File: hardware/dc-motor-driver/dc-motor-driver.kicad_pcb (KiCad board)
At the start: 2 copper layers, 100 x 100 mm, 69 parts, among them J1 DE9, J10 MOT, J12 MOT, J14 MOT, J2 VCC, J4 MOT, J6 MOT, J8 MOT, U1 DRV8874PWPR, U2 DRV8874PWPR, U3 DRV8874PWPR, U4 DRV8874PWPR, U5 DRV8874PWPR, U6 DRV8874PWPR

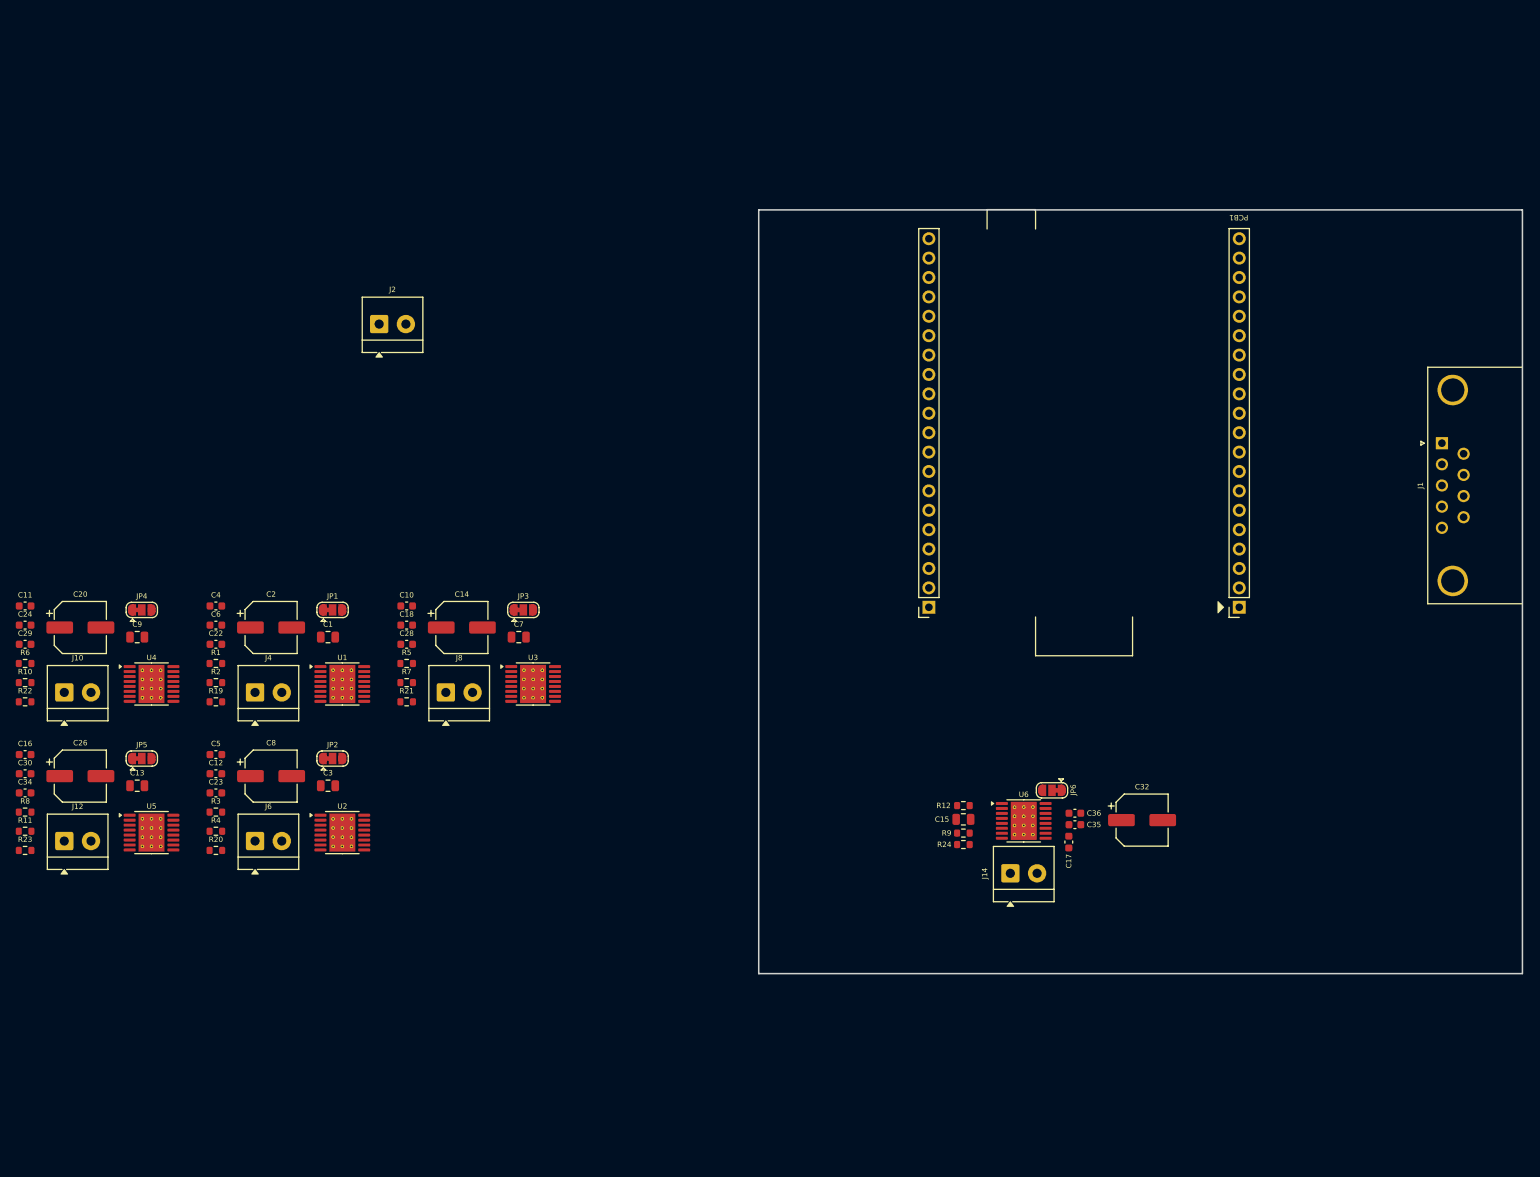
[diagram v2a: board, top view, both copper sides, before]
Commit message: Initial H-Bridge layout with SB footprint added
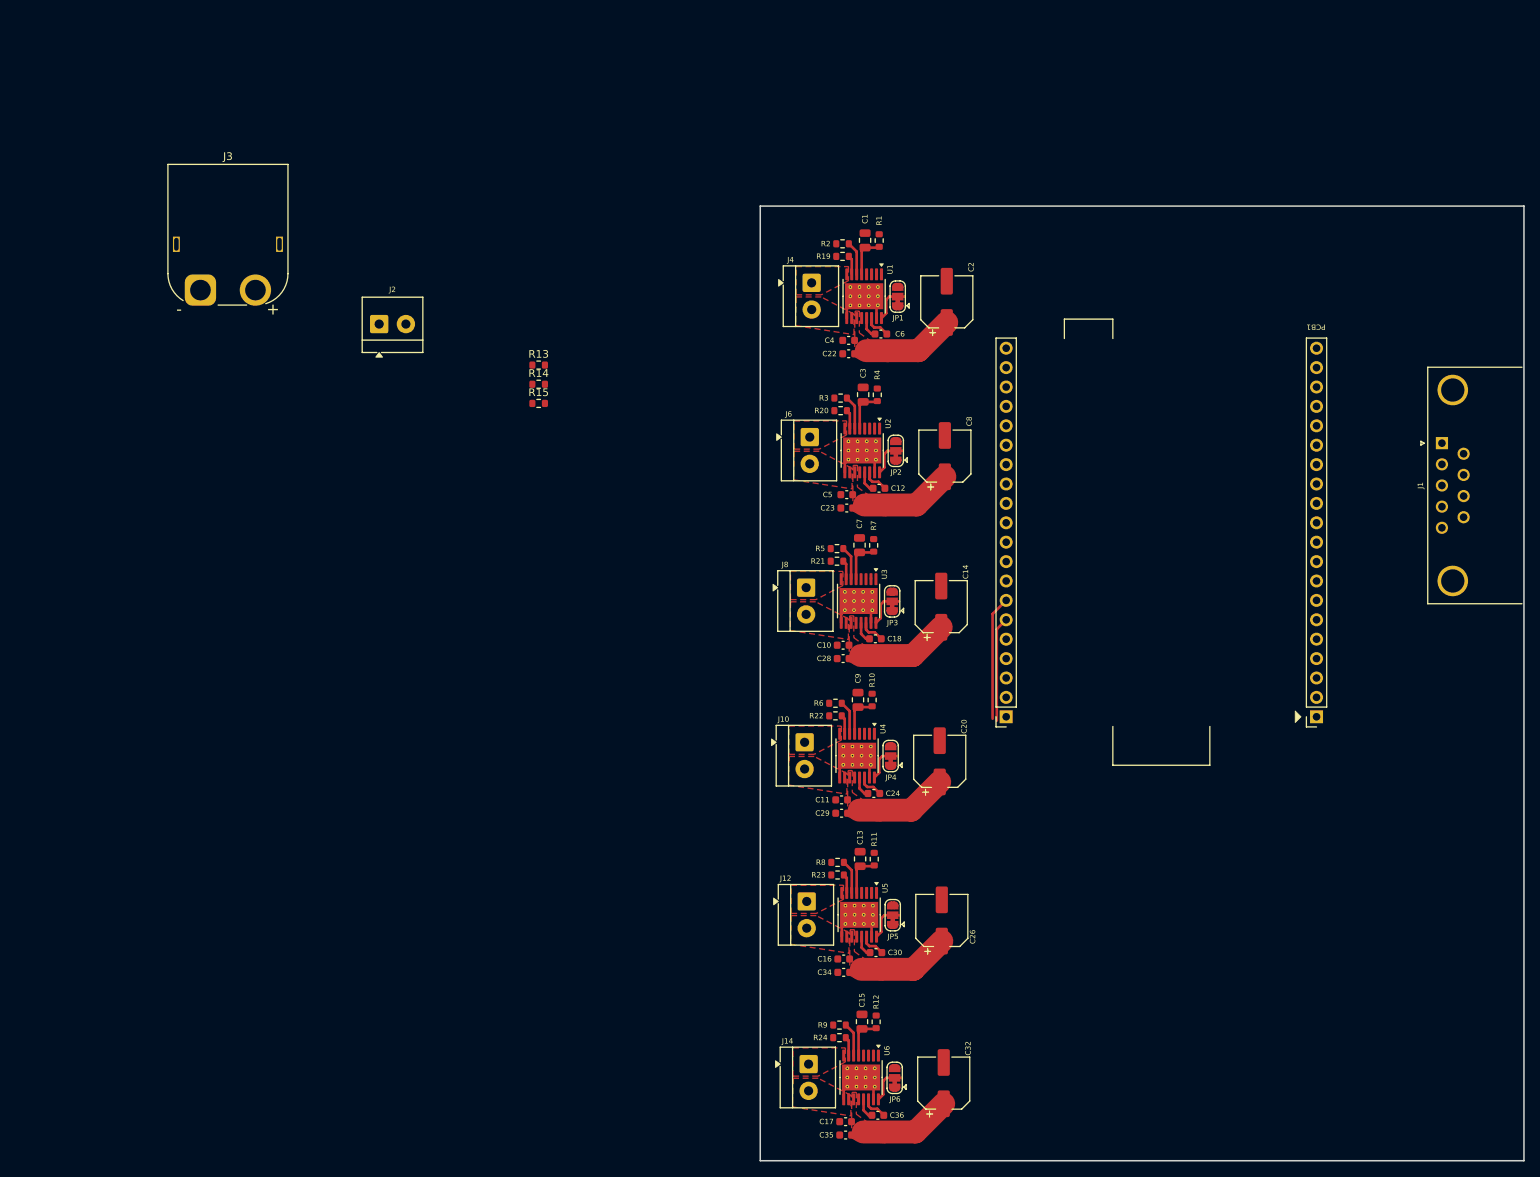
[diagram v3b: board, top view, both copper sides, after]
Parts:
- added J3: Conn_01x02, Connector_AMASS:AMASS_XT60PW-M_1x02_P7.20mm_Horizontal, F.Cu at (42.2, 53.4)
- added R13: 10k, Resistor_SMD:R_0603_1608Metric, F.Cu at (86.5, 63.2)
- added R14: 10k, Resistor_SMD:R_0603_1608Metric, F.Cu at (86.5, 65.7)
- added R15: 10k, Resistor_SMD:R_0603_1608Metric, F.Cu at (86.5, 68.2)
- J2: value VCC -> VIN
- moved C26 114.4 mm to (139.3, 135.9), turned to 90 degrees
- moved C20 113.9 mm to (139.0, 115.1), turned to 90 degrees
- moved C30 113.8 mm to (130.7, 140.2)
- moved C24 113.3 mm to (130.4, 119.3)
- moved R11 111.2 mm to (130.4, 127.9), turned to -90 degrees
- moved R10 110.9 mm to (130.2, 107.1), turned to -90 degrees
- moved C16 110.5 mm to (126.4, 141.0), turned to 180 degrees
- moved C11 109.9 mm to (126.2, 120.2), turned to 180 degrees
- moved C34 109.7 mm to (126.4, 142.7), turned to 180 degrees
- moved C29 109.2 mm to (126.2, 121.9), turned to 180 degrees
- moved R8 106.6 mm to (125.6, 128.3), turned to 180 degrees
- moved R23 106.4 mm to (125.6, 130.0), turned to 180 degrees
- moved R6 106.2 mm to (125.3, 107.5), turned to 180 degrees
- moved R22 106.1 mm to (125.3, 109.2), turned to 180 degrees
- moved R4 103.8 mm to (130.8, 67.1), turned to -90 degrees
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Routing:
- net VCC: track 0.00 -> 72.5 mm
- net GND: track 0.00 -> 21.6 mm
- net /MOT6_IN2: track 0.00 -> 16.4 mm
- net /MOT6_IN1: track 0.00 -> 13.7 mm
- net /BANK1_I_SENSE: track 0.00 -> 8.85 mm
- net /BANK2_I_SENSE: track 0.00 -> 8.85 mm
- net /BANK3_I_SENSE: track 0.00 -> 8.85 mm
- net Net-(U5-VREF): track 0.00 -> 5.58 mm
- net Net-(U4-VREF): track 0.00 -> 5.58 mm
- net Net-(U6-VREF): track 0.00 -> 5.58 mm
- net Net-(U1-VREF): track 0.00 -> 5.58 mm
- net Net-(U3-VREF): track 0.00 -> 5.58 mm
- net Net-(U2-VREF): track 0.00 -> 5.58 mm
- net Net-(JP3-C): track 0.00 -> 5.20 mm
- net Net-(JP6-C): track 0.00 -> 5.20 mm
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- added copper zone on F.Cu, net Net-(J10-Pin_1)
- added copper zone on F.Cu, net Net-(J10-Pin_2)
- added copper zone on F.Cu, net Net-(J12-Pin_1)
- added copper zone on F.Cu, net Net-(J12-Pin_2)
- added copper zone on F.Cu, net Net-(J14-Pin_1)
- added copper zone on F.Cu, net Net-(J14-Pin_2)
- added copper zone on F.Cu, net Net-(J4-Pin_1)
- added copper zone on F.Cu, net Net-(J4-Pin_2)
- added copper zone on F.Cu, net Net-(J6-Pin_1)
- added copper zone on F.Cu, net Net-(J6-Pin_2)
- added copper zone on F.Cu, net Net-(J8-Pin_1)
- added copper zone on F.Cu, net Net-(J8-Pin_2)
- added copper zone on F.Cu, net VCC
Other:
- board size 100 x 100 mm -> 100 x 125 mm

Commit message: feat: DRC rules, more layout done
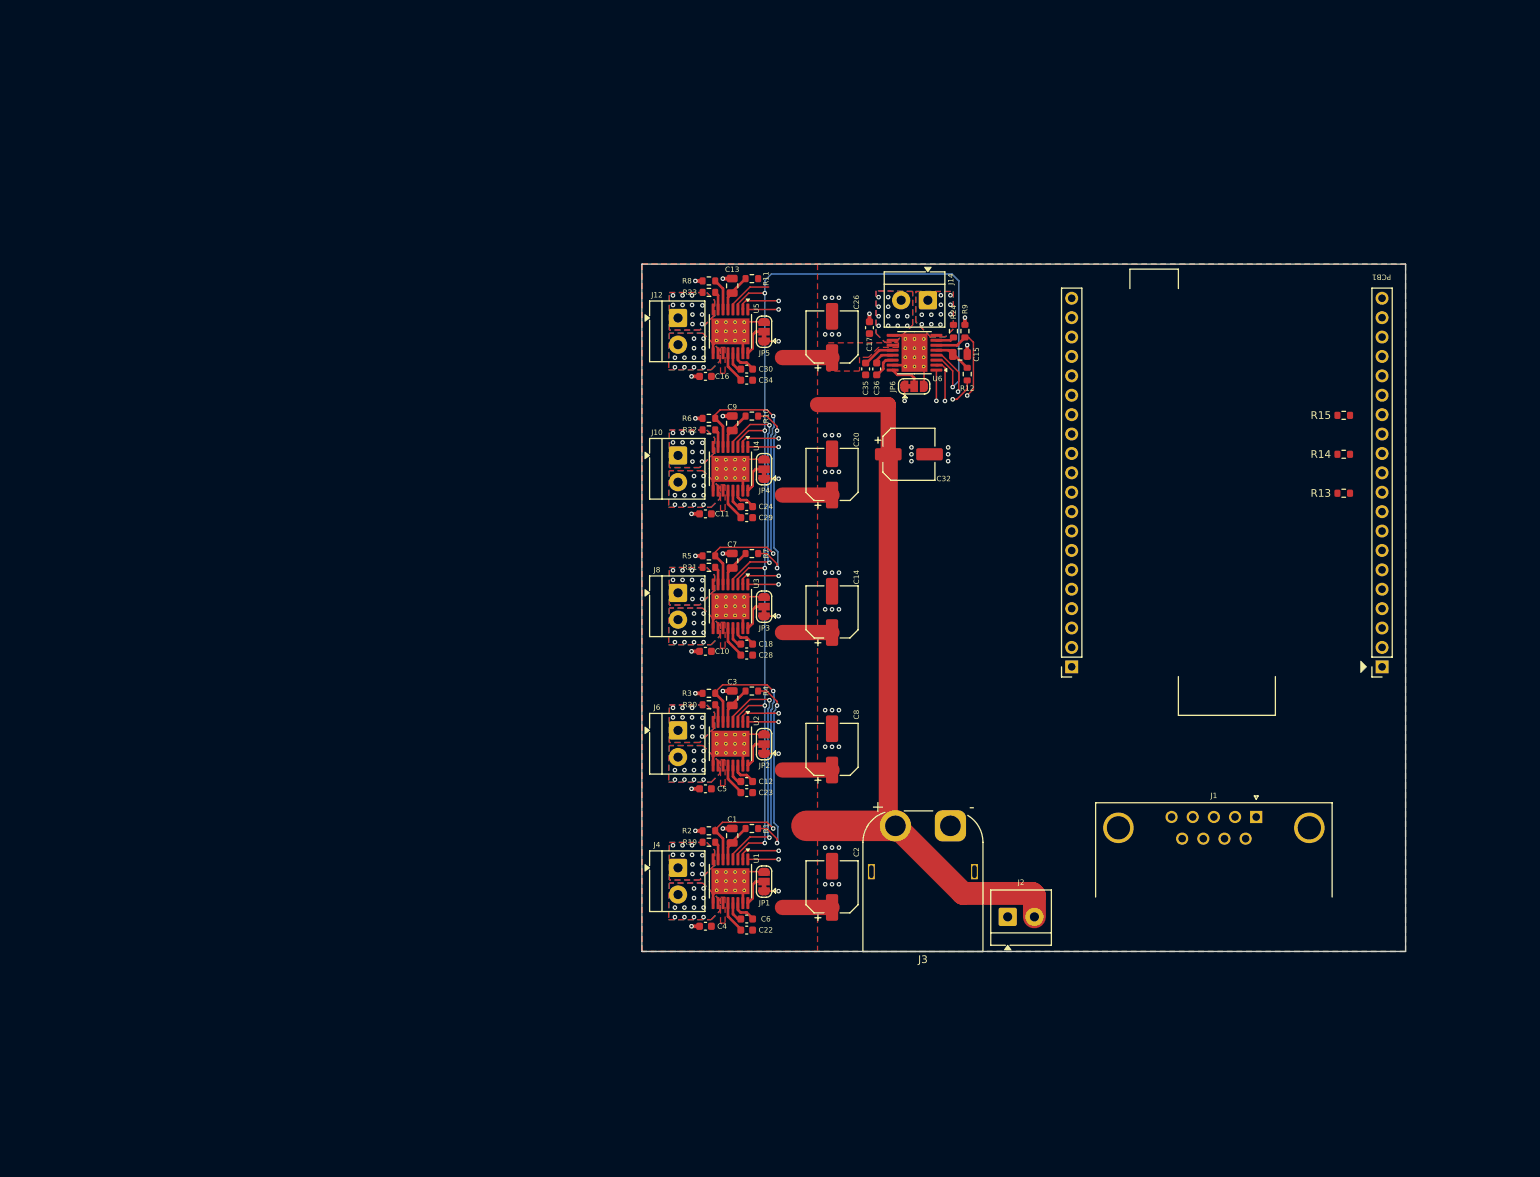
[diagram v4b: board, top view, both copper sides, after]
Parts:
- J3: value Conn_01x02 -> ~
- moved J3 120.7 mm to (140.4, 123.5), turned to 180 degrees
- moved J2 113.1 mm to (147.9, 135.5)
- moved R13 106.7 mm to (191.9, 80.0), turned to 180 degrees
- moved R14 105.8 mm to (191.9, 74.9), turned to 180 degrees
- moved R15 105.4 mm to (191.9, 69.8), turned to 180 degrees
- moved C17 104.0 mm to (129.8, 58.3), turned to 90 degrees
- moved J14 101.2 mm to (137.4, 54.7), turned to 180 degrees
- moved C35 100.3 mm to (129.3, 63.7), turned to 90 degrees
- moved C36 97.7 mm to (130.8, 63.7), turned to -90 degrees
- moved U6 95.2 mm to (135.7, 61.6), turned to 180 degrees
- moved R24 93.7 mm to (140.8, 58.8), turned to 90 degrees
- moved R9 92.3 mm to (142.3, 58.8), turned to 90 degrees
- moved JP6 90.6 mm to (135.7, 66.0), turned to 0 degrees
- moved C15 88.3 mm to (141.7, 61.8), turned to 0 degrees
- moved R12 85.6 mm to (142.6, 64.4), turned to 90 degrees
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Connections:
- J3 pad 1: unconnected-(J3-Pin_1-Pad1) -> GND
- J3 pad 2: unconnected-(J3-Pin_2-Pad2) -> VCC
- PCB1 pad 10: /BANK2_I_SENSE -> /BANK1_~{FLT}
- PCB1 pad 11: /BANK3_I_SENSE -> /BANK2_I_SENSE
- PCB1 pad 12: /BANK1_~{FLT} -> /BANK2_~{FLT}
- PCB1 pad 13: /BANK2_~{FLT} -> /BANK3_I_SENSE
- PCB1 pad 22: /MOT1_IN2 -> /MOT6_IN2
- PCB1 pad 23: /MOT1_IN1 -> /MOT6_IN1
- PCB1 pad 24: /MOT2_IN2 -> /MOT5_IN2
- PCB1 pad 25: /MOT2_IN1 -> /MOT5_IN1
- PCB1 pad 26: /MOT3_IN2 -> /MOT4_IN2
- PCB1 pad 27: /MOT3_IN1 -> /MOT4_IN1
- PCB1 pad 28: /MOT4_IN2 -> /MOT3_IN2
- PCB1 pad 29: /MOT4_IN1 -> /MOT3_IN1
- PCB1 pad 32: /MOT5_IN2 -> /MOT2_IN2
- PCB1 pad 33: /MOT5_IN1 -> /MOT2_IN1
- PCB1 pad 34: /MOT6_IN2 -> /MOT1_IN2
- PCB1 pad 35: /MOT6_IN1 -> /MOT1_IN1
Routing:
- net /~{SLEEP}: track 0.00 -> 143.1 mm, vias 0 -> 6
- net VCC: track 72.5 -> 134.3 mm
- net /BANK1_I_SENSE: track 8.85 -> 44.6 mm, vias 0 -> 2
- net /BANK2_I_SENSE: track 8.85 -> 44.0 mm, vias 0 -> 2
- net GND: track 21.6 -> 56.7 mm, vias 0 -> 54
- net /BANK2_~{FLT}: track 0.00 -> 31.1 mm, vias 0 -> 2
- net /BANK1_~{FLT}: track 0.00 -> 31.1 mm, vias 0 -> 2
- net /BANK1_ILIM: track 0.00 -> 25.6 mm, vias 0 -> 2
- net /BANK2_ILIM: track 0.00 -> 25.6 mm, vias 0 -> 2
- net /BANK3_~{FLT}: track 0.00 -> 12.8 mm, vias 0 -> 1
- net /MOT6_IN2: track 16.4 -> 5.76 mm, vias 0 -> 1
- net /MOT6_IN1: track 13.7 -> 4.03 mm, vias 0 -> 1
- net +3V3: track 0.00 -> 9.14 mm, vias 0 -> 6
- net /BANK3_I_SENSE: track 8.85 -> 17.0 mm, vias 0 -> 1
- net /MOT2_IN2: track 0.15 -> 5.76 mm, vias 0 -> 1
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- added copper zone on B.Cu, net GND
- added copper zone on F.Cu, net GND
- added copper zone on B.Cu, net Net-(J10-Pin_1)
- added copper zone on B.Cu, net Net-(J10-Pin_2)
- added copper zone on B.Cu, net Net-(J12-Pin_1)
- added copper zone on B.Cu, net Net-(J12-Pin_2)
- added copper zone on B.Cu, net Net-(J14-Pin_1)
- added copper zone on B.Cu, net Net-(J14-Pin_2)
- added copper zone on B.Cu, net Net-(J4-Pin_1)
- added copper zone on B.Cu, net Net-(J4-Pin_2)
- added copper zone on B.Cu, net Net-(J6-Pin_1)
- added copper zone on B.Cu, net Net-(J6-Pin_2)
- added copper zone on B.Cu, net Net-(J8-Pin_1)
- added copper zone on B.Cu, net Net-(J8-Pin_2)
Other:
- board size 100 x 125 mm -> 100 x 90 mm
- rule pad_to_mask_clearance: 0 -> 0.038

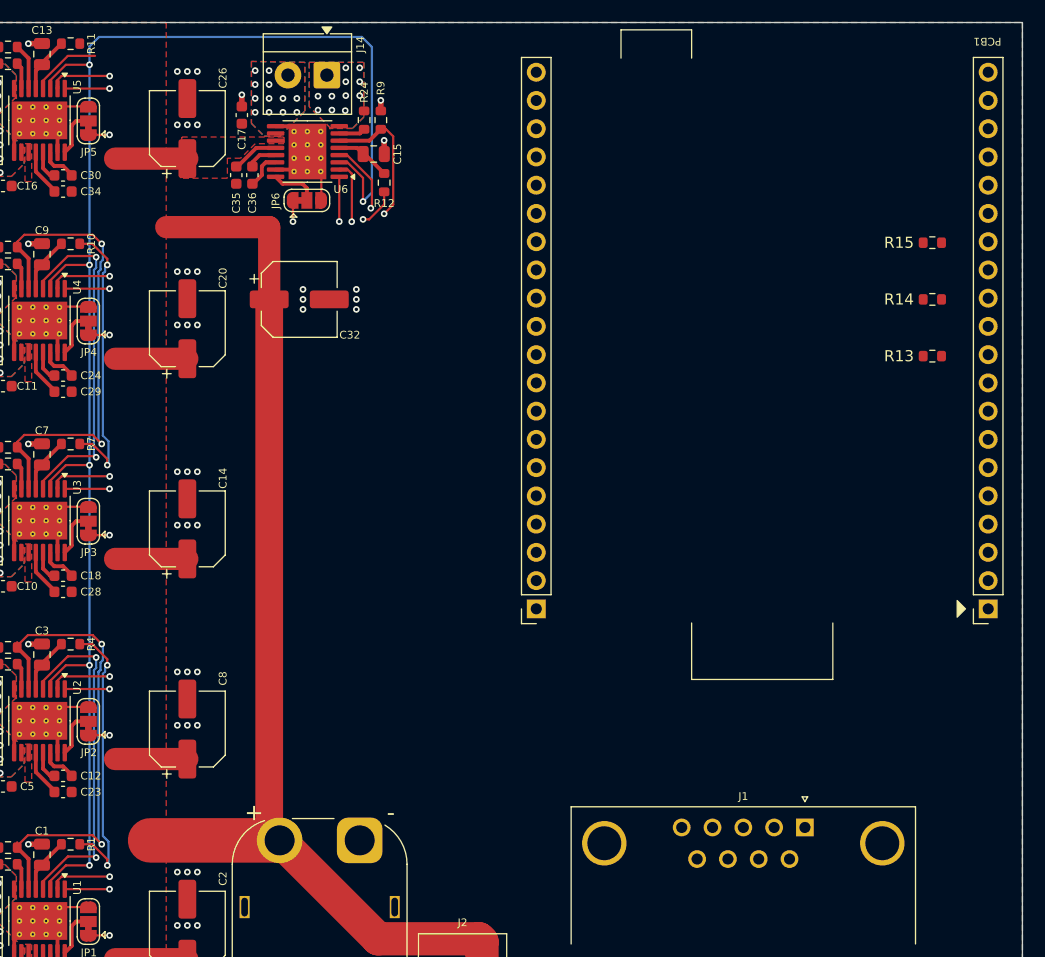
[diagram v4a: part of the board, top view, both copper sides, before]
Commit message: Rough routing of motor_in for H-bridges
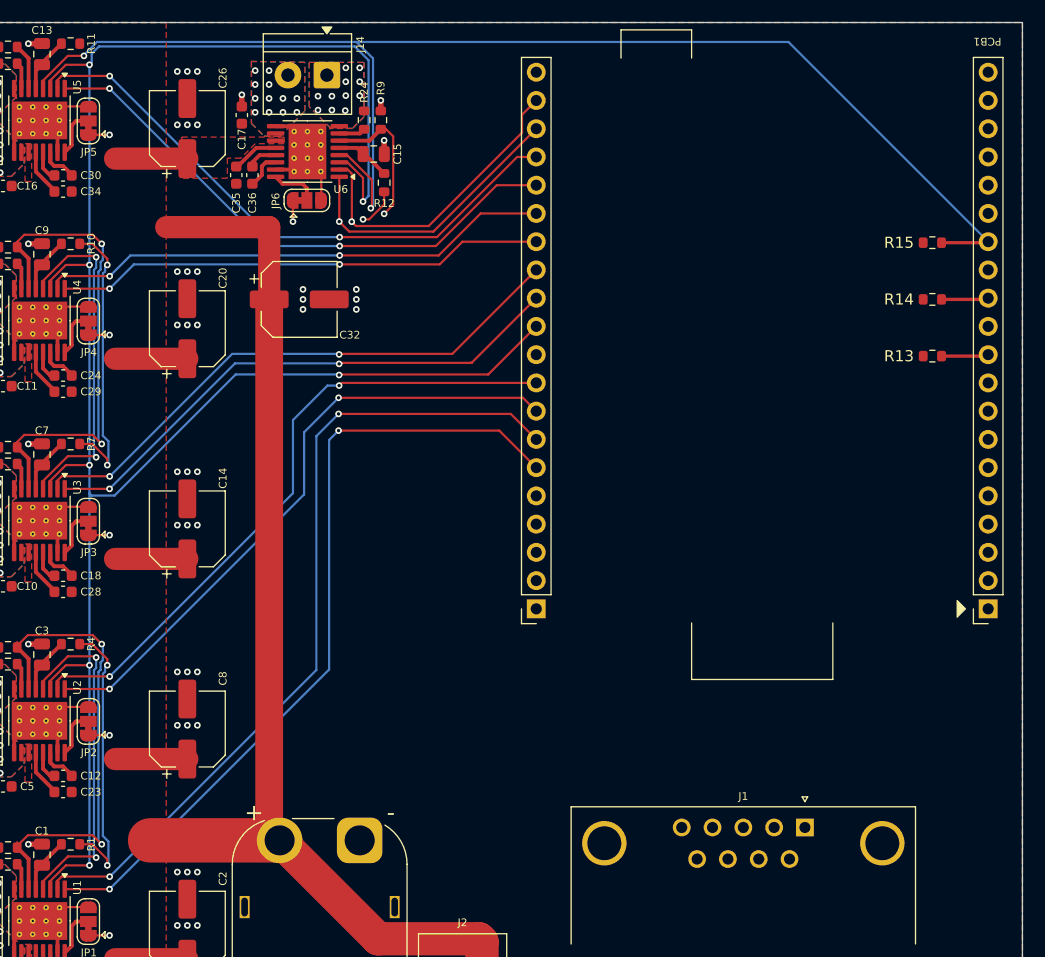
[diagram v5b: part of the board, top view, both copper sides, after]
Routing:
- net /BANK3_~{FLT}: track 12.8 -> 121.0 mm, vias 1 -> 2
- net /MOT1_IN1: track 4.03 -> 73.0 mm, vias 1 -> 2
- net /MOT1_IN2: track 5.76 -> 74.6 mm, vias 1 -> 2
- net /MOT2_IN2: track 5.76 -> 58.9 mm, vias 1 -> 2
- net /MOT2_IN1: track 4.03 -> 57.0 mm, vias 1 -> 2
- net /MOT5_IN2: track 5.76 -> 53.1 mm, vias 1 -> 2
- net /MOT5_IN1: track 4.03 -> 50.6 mm, vias 1 -> 2
- net /MOT3_IN2: track 5.76 -> 51.9 mm, vias 1 -> 2
- net /MOT3_IN1: track 4.03 -> 49.7 mm, vias 1 -> 2
- net /~{SLEEP}: track 143.1 -> 187.3 mm, vias 6 -> 7
- net /MOT4_IN2: track 5.76 -> 46.5 mm, vias 1 -> 2
- net /MOT4_IN1: track 4.03 -> 44.2 mm, vias 1 -> 2
- net /MOT6_IN2: track 5.76 -> 28.1 mm
- net /MOT6_IN1: track 4.03 -> 25.9 mm
- net /BANK1_~{FLT}: track 31.1 -> 35.3 mm
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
